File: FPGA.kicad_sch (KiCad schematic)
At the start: 19 parts, among them U10 FPGA_GPIO_Extra, U3 XC7A100T-FTG256, U5 S25FL127S, U6 Oscillator, U7 FPGA_JTAG_Debug

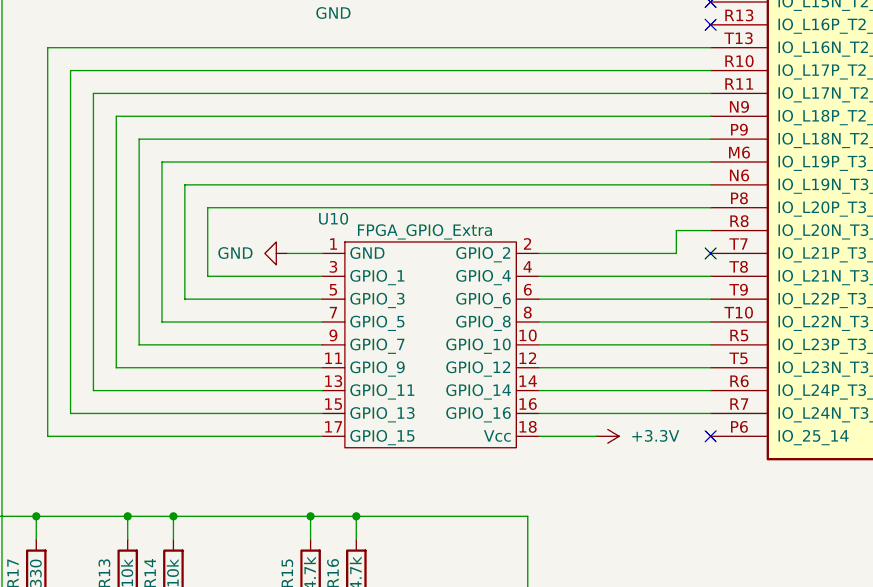
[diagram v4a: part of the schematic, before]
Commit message: Rewired FPGA GPIO out for easier PCB wiring
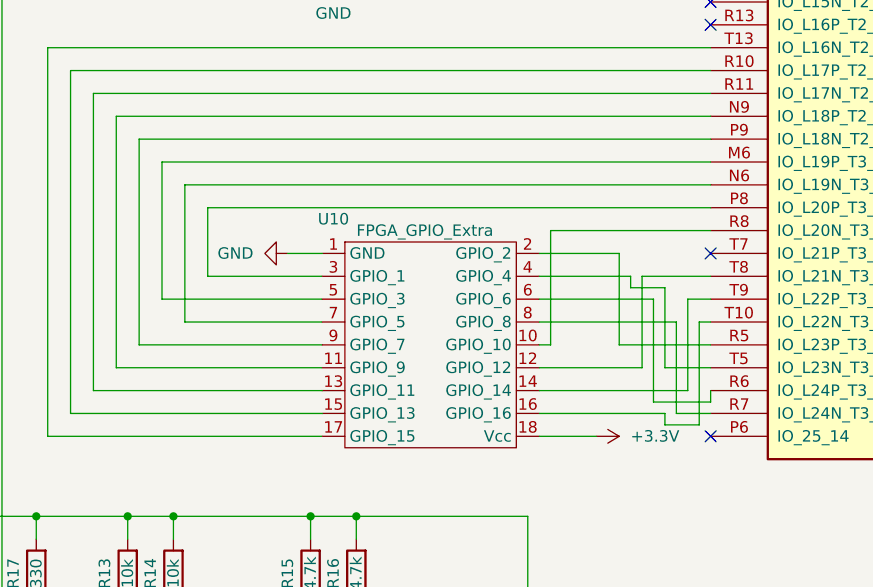
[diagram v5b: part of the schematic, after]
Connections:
- net at U3.M6 (IO_L19P_T3_A10_D26_14): now also U10.5 (GPIO_3); no longer U10.7 (GPIO_5)
- net at U3.N6 (IO_L19N_T3_A09_D25_VREF_14): now also U10.7 (GPIO_5); no longer U10.5 (GPIO_3)
- net at U3.R5 (IO_L23P_T3_A03_D19_14): now also U10.2 (GPIO_2); no longer U10.10 (GPIO_10)
- net at U3.R6 (IO_L24P_T3_A01_D17_14): now also U10.6 (GPIO_6); no longer U10.14 (GPIO_14)
- net at U3.R7 (IO_L24N_T3_A00_D16_14): now also U10.8 (GPIO_8); no longer U10.16 (GPIO_16)
- net at U3.R8 (IO_L20N_T3_A07_D23_14): now also U10.10 (GPIO_10); no longer U10.2 (GPIO_2)
- net at U3.T10 (IO_L22N_T3_A04_D20_14): now also U10.16 (GPIO_16); no longer U10.8 (GPIO_8)
- net at U3.T5 (IO_L23N_T3_A02_D18_14): now also U10.4 (GPIO_4); no longer U10.12 (GPIO_12)
- net at U3.T8 (IO_L21N_T3_DQS_A06_D22_14): now also U10.12 (GPIO_12); no longer U10.4 (GPIO_4)
- net at U3.T9 (IO_L22P_T3_A05_D21_14): now also U10.14 (GPIO_14); no longer U10.6 (GPIO_6)
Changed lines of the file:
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@@
+    (stroke (width 0) (type default))
+  )
+  (wire (pts (xy 180.34 171.45) (xy 180.34 161.29))
     (stroke (width 0) (type default))
   )
@@
     (stroke (width 0) (type default))
   )
-  (wire (pts (xy 165.1 153.67) (xy 180.34 153.67))
-    (stroke (width 0) (type default))
-  )
   (wire (pts (xy 101.6 210.82) (xy 119.38 210.82))
     (stroke (width 0) (type default))
@@
     (stroke (width 0) (type default))
   )
+  (wire (pts (xy 177.8 158.75) (xy 177.8 170.18))
+    (stroke (width 0) (type default))
+  )
   (wire (pts (xy 102.87 248.92) (xy 102.87 254))
     (stroke (width 0) (type default))
@@
     (stroke (width 0) (type default))
   )
+  (wire (pts (xy 175.26 157.48) (xy 175.26 156.21))
+    (stroke (width 0) (type default))
+  )
   (wire (pts (xy 289.56 207.01) (xy 288.29 207.01))
     (stroke (width 0) (type default))
@@
     (stroke (width 0) (type default))
   )
-  (wire (pts (xy 165.1 163.83) (xy 184.15 163.83))
-    (stroke (width 0) (type default))
-  )
   (wire (pts (xy 106.68 229.87) (xy 106.68 231.14))
     (stroke (width 0) (type default))
@@
     (stroke (width 0) (type default))
   )
-  (wire (pts (xy 123.19 143.51) (xy 123.19 161.29))
+  (wire (pts (xy 123.19 143.51) (xy 123.19 158.75))
+    (stroke (width 0) (type default))
+  )
+  (wire (pts (xy 179.07 171.45) (xy 165.1 171.45))
     (stroke (width 0) (type default))
   )
@@
     (stroke (width 0) (type default))
   )
+  (wire (pts (xy 184.15 158.75) (xy 181.61 158.75))
+    (stroke (width 0) (type default))
+  )
   (wire (pts (xy 120.65 140.97) (xy 184.15 140.97))
     (stroke (width 0) (type default))
@@
     (stroke (width 0) (type default))
   )
-  (wire (pts (xy 165.1 166.37) (xy 184.15 166.37))
-    (stroke (width 0) (type default))
-  )
   (wire (pts (xy 236.22 260.35) (xy 237.49 260.35))
     (stroke (width 0) (type default))
@@
     (stroke (width 0) (type default))
   )
-  (wire (pts (xy 165.1 161.29) (xy 184.15 161.29))
-    (stroke (width 0) (type default))
-  )
   (wire (pts (xy 168.91 228.6) (xy 127 228.6))
     (stroke (width 0) (type default))
@@
     (stroke (width 0) (type default))
   )
+  (wire (pts (xy 184.15 168.91) (xy 184.15 170.18))
+    (stroke (width 0) (type default))
+  )
+  (wire (pts (xy 173.99 163.83) (xy 184.15 163.83))
+    (stroke (width 0) (type default))
+  )
   (wire (pts (xy 147.32 77.47) (xy 184.15 77.47))
     (stroke (width 0) (type default))
@@
     (stroke (width 0) (type default))
   )
+  (wire (pts (xy 165.1 163.83) (xy 166.37 163.83))
+    (stroke (width 0) (type default))
+  )
   (wire (pts (xy 151.13 107.95) (xy 151.13 115.57))
     (stroke (width 0) (type default))
@@
     (stroke (width 0) (type default))
   )
+  (wire (pts (xy 173.99 163.83) (xy 173.99 153.67))
+    (stroke (width 0) (type default))
+  )
   (wire (pts (xy 182.88 100.33) (xy 182.88 101.6))
     (stroke (width 0) (type default))
   )
+  (wire (pts (xy 165.1 153.67) (xy 173.99 153.67))
+    (stroke (width 0) (type default))
+  )
   (wire (pts (xy 66.04 81.28) (xy 66.04 82.55))
     (stroke (width 0) (type default))
   )
-  (wire (pts (xy 123.19 161.29) (xy 140.97 161.29))
-    (stroke (width 0) (type default))
-  )
   (wire (pts (xy 177.8 90.17) (xy 184.15 90.17))
     (stroke (width 0) (type default))
@@
     (stroke (width 0) (type default))
   )
+  (wire (pts (xy 182.88 161.29) (xy 182.88 172.72))
+    (stroke (width 0) (type default))
+  )
   (wire (pts (xy 179.07 67.31) (xy 184.15 67.31))
     (stroke (width 0) (type default))
@@
     (stroke (width 0) (type default))
   )
+  (wire (pts (xy 184.15 161.29) (xy 182.88 161.29))
+    (stroke (width 0) (type default))
+  )
   (wire (pts (xy 289.56 209.55) (xy 289.56 212.09))
     (stroke (width 0) (type default))
@@
     (stroke (width 0) (type default))
   )
-  (wire (pts (xy 184.15 151.13) (xy 180.34 151.13))
+  (wire (pts (xy 182.88 172.72) (xy 179.07 172.72))
+    (stroke (width 0) (type default))
+  )
+  (wire (pts (xy 166.37 151.13) (xy 184.15 151.13))
     (stroke (width 0) (type default))
   )
@@
     (stroke (width 0) (type default))
   )
+  (wire (pts (xy 177.8 158.75) (xy 165.1 158.75))
+    (stroke (width 0) (type default))
+  )
   (wire (pts (xy 262.89 27.94) (xy 265.43 27.94))
     (stroke (width 0) (type default))
@@
     (stroke (width 0) (type default))
   )
+  (wire (pts (xy 125.73 161.29) (xy 140.97 161.29))
+    (stroke (width 0) (type default))
+  )
   (wire (pts (xy 125.73 146.05) (xy 184.15 146.05))
     (stroke (width 0) (type default))
@@
     (stroke (width 0) (type default))
   )
+  (wire (pts (xy 184.15 156.21) (xy 176.53 156.21))
+    (stroke (width 0) (type default))
+  )
   (wire (pts (xy 237.49 214.63) (xy 220.98 214.63))
     (stroke (width 0) (type default))
@@
     (stroke (width 0) (type default))
   )
+  (wire (pts (xy 123.19 158.75) (xy 140.97 158.75))
+    (stroke (width 0) (type default))
+  )
   (wire (pts (xy 236.22 237.49) (xy 236.22 240.03))
     (stroke (width 0) (type default))
@@
     (stroke (width 0) (type default))
   )
-  (wire (pts (xy 125.73 146.05) (xy 125.73 158.75))
+  (wire (pts (xy 125.73 146.05) (xy 125.73 161.29))
+    (stroke (width 0) (type default))
+  )
+  (wire (pts (xy 175.26 156.21) (xy 165.1 156.21))
     (stroke (width 0) (type default))
   )
@@
     (stroke (width 0) (type default))
   )
+  (wire (pts (xy 179.07 166.37) (xy 179.07 157.48))
+    (stroke (width 0) (type default))
+  )
   (wire (pts (xy 381 29.21) (xy 381 34.29))
     (stroke (width 0) (type default))
@@
     (stroke (width 0) (type default))
   )
+  (wire (pts (xy 179.07 172.72) (xy 179.07 171.45))
+    (stroke (width 0) (type default))
+  )
   (wire (pts (xy 236.22 255.27) (xy 237.49 255.27))
     (stroke (width 0) (type default))
@@
     (stroke (width 0) (type default))
   )
-  (wire (pts (xy 125.73 158.75) (xy 140.97 158.75))
-    (stroke (width 0) (type default))
-  )
   (wire (pts (xy 289.56 265.43) (xy 289.56 267.97))
     (stroke (width 0) (type default))
@@
     (stroke (width 0) (type default))
   )
+  (wire (pts (xy 184.15 171.45) (xy 180.34 171.45))
+    (stroke (width 0) (type default))
+  )
   (wire (pts (xy 60.96 64.77) (xy 147.32 64.77))
     (stroke (width 0) (type default))
@@
     (stroke (width 0) (type default))
   )
+  (wire (pts (xy 177.8 170.18) (xy 184.15 170.18))
+    (stroke (width 0) (type default))
+  )
   (wire (pts (xy 110.49 173.99) (xy 140.97 173.99))
     (stroke (width 0) (type default))
@@
     (stroke (width 0) (type default))
   )
+  (wire (pts (xy 166.37 151.13) (xy 166.37 163.83))
+    (stroke (width 0) (type default))
+  )
   (wire (pts (xy 289.56 252.73) (xy 288.29 252.73))
     (stroke (width 0) (type default))
@@
     (stroke (width 0) (type default))
   )
+  (wire (pts (xy 180.34 161.29) (xy 165.1 161.29))
+    (stroke (width 0) (type default))
+  )
   (wire (pts (xy 110.49 59.69) (xy 110.49 73.66))
     (stroke (width 0) (type default))
@@
     (stroke (width 0) (type default))
   )
+  (wire (pts (xy 179.07 157.48) (xy 175.26 157.48))
+    (stroke (width 0) (type default))
+  )
   (wire (pts (xy 119.38 182.88) (xy 124.46 182.88))
     (stroke (width 0) (type default))
@@
     (stroke (width 0) (type default))
   )
+  (wire (pts (xy 181.61 158.75) (xy 181.61 168.91))
+    (stroke (width 0) (type default))
+  )
   (wire (pts (xy 118.11 138.43) (xy 118.11 166.37))
     (stroke (width 0) (type default))
   )
-  (wire (pts (xy 180.34 151.13) (xy 180.34 153.67))
-    (stroke (width 0) (type default))
-  )
   (wire (pts (xy 182.88 101.6) (xy 180.34 101.6))
     (stroke (width 0) (type default))
   )
-  (wire (pts (xy 165.1 158.75) (xy 184.15 158.75))
-    (stroke (width 0) (type default))
-  )
   (wire (pts (xy 236.22 222.25) (xy 237.49 222.25))
     (stroke (width 0) (type default))
@@
     (stroke (width 0) (type default))
   )
+  (wire (pts (xy 176.53 156.21) (xy 176.53 166.37))
+    (stroke (width 0) (type default))
+  )
   (wire (pts (xy 105.41 45.72) (xy 110.49 45.72))
     (stroke (width 0) (type default))
@@
     (stroke (width 0) (type default))
   )
-  (wire (pts (xy 165.1 168.91) (xy 184.15 168.91))
-    (stroke (width 0) (type default))
-  )
   (wire (pts (xy 236.22 240.03) (xy 236.22 242.57))
     (stroke (width 0) (type default))
@@
     (stroke (width 0) (type default))
   )
-  (wire (pts (xy 165.1 156.21) (xy 184.15 156.21))
+  (wire (pts (xy 165.1 168.91) (xy 181.61 168.91))
+    (stroke (width 0) (type default))
+  )
+  (wire (pts (xy 184.15 166.37) (xy 179.07 166.37))
+    (stroke (width 0) (type default))
+  )
+  (wire (pts (xy 176.53 166.37) (xy 165.1 166.37))
     (stroke (width 0) (type default))
   )
@@
     (stroke (width 0) (type default))
   )
-  (wire (pts (xy 165.1 171.45) (xy 184.15 171.45))
-    (stroke (width 0) (type default))
-  )

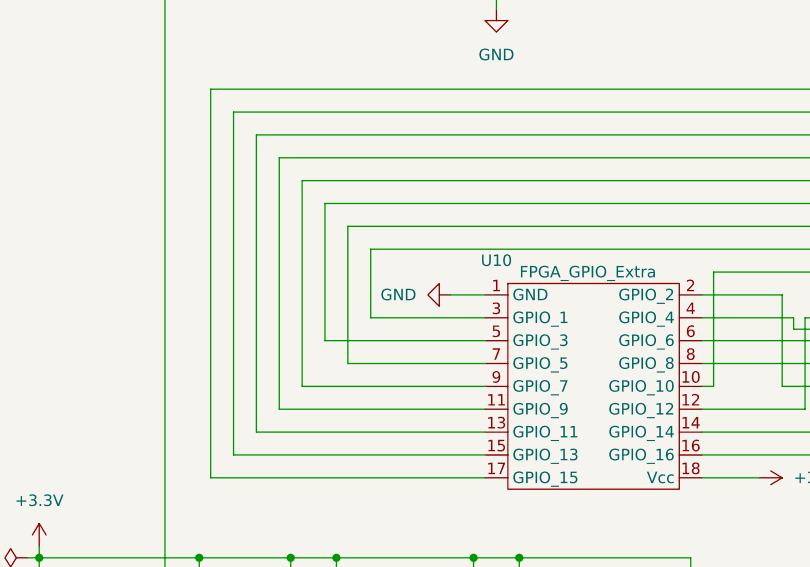
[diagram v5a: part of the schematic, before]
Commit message: Added 1V0 layer, Increased heatsinks
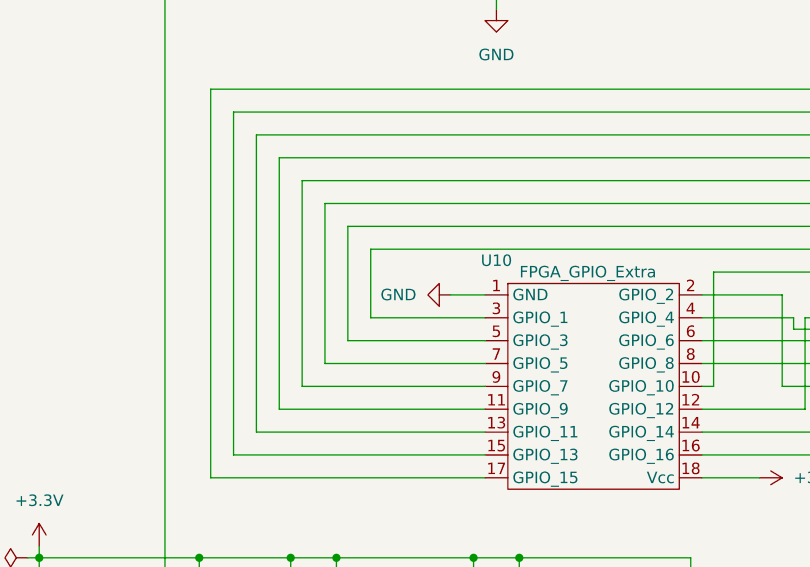
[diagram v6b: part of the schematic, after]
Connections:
- net at U3.M6 (IO_L19P_T3_A10_D26_14): now also U10.7 (GPIO_5); no longer U10.5 (GPIO_3)
- net at U3.N6 (IO_L19N_T3_A09_D25_VREF_14): now also U10.5 (GPIO_3); no longer U10.7 (GPIO_5)
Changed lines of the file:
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@@
-    (stroke (width 0) (type default))
-  )
-  (wire (pts (xy 123.19 143.51) (xy 123.19 158.75))
     (stroke (width 0) (type default))
   )
@@
     (stroke (width 0) (type default))
   )
+  (wire (pts (xy 140.97 161.29) (xy 123.19 161.29))
+    (stroke (width 0) (type default))
+  )
   (wire (pts (xy 289.56 204.47) (xy 289.56 207.01))
     (stroke (width 0) (type default))
@@
     (stroke (width 0) (type default))
   )
-  (wire (pts (xy 125.73 161.29) (xy 140.97 161.29))
-    (stroke (width 0) (type default))
-  )
   (wire (pts (xy 125.73 146.05) (xy 184.15 146.05))
     (stroke (width 0) (type default))
@@
     (stroke (width 0) (type default))
   )
-  (wire (pts (xy 123.19 158.75) (xy 140.97 158.75))
-    (stroke (width 0) (type default))
-  )
   (wire (pts (xy 236.22 237.49) (xy 236.22 240.03))
     (stroke (width 0) (type default))
@@
     (stroke (width 0) (type default))
   )
-  (wire (pts (xy 125.73 146.05) (xy 125.73 161.29))
+  (wire (pts (xy 125.73 146.05) (xy 125.73 158.75))
     (stroke (width 0) (type default))
   )
@@
     (stroke (width 0) (type default))
   )
+  (wire (pts (xy 123.19 143.51) (xy 123.19 161.29))
+    (stroke (width 0) (type default))
+  )
   (wire (pts (xy 168.91 226.06) (xy 129.54 226.06))
     (stroke (width 0) (type default))
@@
     (stroke (width 0) (type default))
   )
+  (wire (pts (xy 125.73 158.75) (xy 140.97 158.75))
+    (stroke (width 0) (type default))
+  )
